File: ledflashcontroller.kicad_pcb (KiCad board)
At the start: 2 copper layers, 100 x 100 mm, 72 parts, among them J1 Conn_02x08_Odd_Even, J2 CONN_01X02, J3 CONN_01X02, J4 Conn_01x02, K1 LDD-1000H, K2 LDD-1000H, P1 V_IN, P10 BNC, P11 BNC, P12 BNC, P2 I2C_HEADER, P3 GPIO_HEADER, P4 V_DIM1, P5 V_DIM2, P6 V_OUT, P7 BNC, P8 BNC, P9 BNC, Q1 IRLML6244, Q2 IRFB3256, U1 Teensy3.6, U10 DMC2700, U11 DS3231, U2 ISO1540, U3 DMC2700, U4 DMC2700, U5 ISO1540, U6 DMC2700, U7 DMC2700, U8 ISO1540, U9 DMC2700

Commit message: Minor change in wireing
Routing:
- net /TRIG_IO1: track 59.8 -> 37.7 mm, vias 1 -> 3
- net GND: track 693.8 -> 692.6 mm
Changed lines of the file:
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@@
     (links 224)
     (no_connects 0)
-    (area 29.924999 29.924999 130.075001 130.075001)
+    (area 29.664999 26.418399 142.064286 151.875001)
     (thickness 1.6)
     (drawings 8)
-    (tracks 998)
+    (tracks 997)
     (zones 0)
     (modules 72)
@@
     (add_net GND)
   )
+  (module lib_fp:LDD-1000H (layer F.Cu)
+    (at 48.16 62.12 90)
+    (descr LDD-1000H)
+    (tags "Relay or Contactor")
+    (fp_text reference K1 (at -0.44814 0.04874 90) (layer F.SilkS)
+      (effects (font (size 1.27 1.27) (thickness 0.254)))
+    )
+    (fp_text value LDD-1000H (at -0.44814 0.04874 90) (layer F.SilkS) hide
+      (effects (font (size 1.27 1.27) (thickness 0.254)))
+    )
+    (fp_line (start -10.15 -15.9) (end 10.15 -15.9) (layer Dwgs.User) (width 0.254))
+    (fp_line (start 10.15 -15.9) (end 10.15 15.9) (layer Dwgs.User) (width 0.254))
+    (fp_line (start 10.15 15.9) (end -10.15 15.9) (layer Dwgs.User) (width 0.254))
+    (fp_line (start -10.15 15.9) (end -10.15 -15.9) (layer Dwgs.User) (width 0.254))
+    (fp_line (start -10.15 15.9) (end -10.15 -15.9) (layer F.SilkS) (width 0.254))
+    (fp_line (start -10.15 -15.9) (end 10.15 -15.9) (layer F.SilkS) (width 0.254))
+    (fp_line (start 10.15 -15.9) (end 10.15 15.9) (layer F.SilkS) (width 0.254))
+    (fp_line (start 10.15 15.9) (end -10.15 15.9) (layer F.SilkS) (width 0.254))
+    (fp_circle (center -11.382 -14.057) (end -11.55687 -14.057) (layer F.SilkS) (width 0.254))
+    (pad 1 thru_hole circle (at -7.62 -13.84 180) (size 1.3 1.3) (drill 0.8) (layers *.Cu *.Mask F.SilkS)
+      (net 2 GND))
+    (pad 1 thru_hole circle (at -7.62 -11.3 180) (size 1.3 1.3) (drill 0.8) (layers *.Cu *.Mask F.SilkS)
+      (net 2 GND))
+    (pad 23 thru_hole circle (at 7.62 -13.84 180) (size 1.3 1.3) (drill 0.8) (layers *.Cu *.Mask F.SilkS)
+      (net 16 +48V))
+    (pad 23 thru_hole circle (at 7.62 -11.3 180) (size 1.3 1.3) (drill 0.8) (layers *.Cu *.Mask F.SilkS)
+      (net 16 +48V))
+    (pad 22 thru_hole circle (at 7.62 -8.76 180) (size 1.3 1.3) (drill 0.8) (layers *.Cu *.Mask F.SilkS)
+      (net 3 "Net-(K1-Pad22)"))
+    (pad 11 thru_hole circle (at -7.62 11.3 180) (size 1.3 1.3) (drill 0.8) (layers *.Cu *.Mask F.SilkS)
+      (net 4 "Net-(K1-Pad11)"))
+    (pad 11 thru_hole circle (at -7.62 13.84 180) (size 1.3 1.3) (drill 0.8) (layers *.Cu *.Mask F.SilkS)
+      (net 4 "Net-(K1-Pad11)"))
+    (pad 13 thru_hole circle (at 7.62 11.3 180) (size 1.3 1.3) (drill 0.8) (layers *.Cu *.Mask F.SilkS)
+      (net 5 "Net-(K1-Pad13)"))
+    (pad 13 thru_hole circle (at 7.62 13.84 180) (size 1.3 1.3) (drill 0.8) (layers *.Cu *.Mask F.SilkS)
+      (net 5 "Net-(K1-Pad13)"))
+  )
   (module lib_fp:Teensy35_36_no_center (layer F.Cu)
     (at 62.09 88.62)
@@
     )
   )
-  (module lib_fp:LDD-1000H (layer F.Cu)
-    (at 48.16 62.12 90)
-    (descr LDD-1000H)
-    (tags "Relay or Contactor")
-    (fp_text reference K1 (at -0.44814 0.04874 90) (layer F.SilkS)
-      (effects (font (size 1.27 1.27) (thickness 0.254)))
-    )
-    (fp_text value LDD-1000H (at -0.44814 0.04874 90) (layer F.SilkS) hide
-      (effects (font (size 1.27 1.27) (thickness 0.254)))
-    )
-    (fp_line (start -10.15 -15.9) (end 10.15 -15.9) (layer Dwgs.User) (width 0.254))
-    (fp_line (start 10.15 -15.9) (end 10.15 15.9) (layer Dwgs.User) (width 0.254))
-    (fp_line (start 10.15 15.9) (end -10.15 15.9) (layer Dwgs.User) (width 0.254))
-    (fp_line (start -10.15 15.9) (end -10.15 -15.9) (layer Dwgs.User) (width 0.254))
-    (fp_line (start -10.15 15.9) (end -10.15 -15.9) (layer F.SilkS) (width 0.254))
-    (fp_line (start -10.15 -15.9) (end 10.15 -15.9) (layer F.SilkS) (width 0.254))
-    (fp_line (start 10.15 -15.9) (end 10.15 15.9) (layer F.SilkS) (width 0.254))
-    (fp_line (start 10.15 15.9) (end -10.15 15.9) (layer F.SilkS) (width 0.254))
-    (fp_circle (center -11.382 -14.057) (end -11.55687 -14.057) (layer F.SilkS) (width 0.254))
-    (pad 1 thru_hole circle (at -7.62 -13.84 180) (size 1.3 1.3) (drill 0.8) (layers *.Cu *.Mask F.SilkS)
-      (net 2 GND))
-    (pad 1 thru_hole circle (at -7.62 -11.3 180) (size 1.3 1.3) (drill 0.8) (layers *.Cu *.Mask F.SilkS)
-      (net 2 GND))
-    (pad 23 thru_hole circle (at 7.62 -13.84 180) (size 1.3 1.3) (drill 0.8) (layers *.Cu *.Mask F.SilkS)
-      (net 16 +48V))
-    (pad 23 thru_hole circle (at 7.62 -11.3 180) (size 1.3 1.3) (drill 0.8) (layers *.Cu *.Mask F.SilkS)
-      (net 16 +48V))
-    (pad 22 thru_hole circle (at 7.62 -8.76 180) (size 1.3 1.3) (drill 0.8) (layers *.Cu *.Mask F.SilkS)
-      (net 3 "Net-(K1-Pad22)"))
-    (pad 11 thru_hole circle (at -7.62 11.3 180) (size 1.3 1.3) (drill 0.8) (layers *.Cu *.Mask F.SilkS)
-      (net 4 "Net-(K1-Pad11)"))
-    (pad 11 thru_hole circle (at -7.62 13.84 180) (size 1.3 1.3) (drill 0.8) (layers *.Cu *.Mask F.SilkS)
-      (net 4 "Net-(K1-Pad11)"))
-    (pad 13 thru_hole circle (at 7.62 11.3 180) (size 1.3 1.3) (drill 0.8) (layers *.Cu *.Mask F.SilkS)
-      (net 5 "Net-(K1-Pad13)"))
-    (pad 13 thru_hole circle (at 7.62 13.84 180) (size 1.3 1.3) (drill 0.8) (layers *.Cu *.Mask F.SilkS)
-      (net 5 "Net-(K1-Pad13)"))
-  )
   (module Resistors_SMD:R_1206_HandSoldering (layer F.Cu)
     (at 124 107)
@@
   (segment (start 44 108.95) (end 44 111) (width 0.4) (layer F.Cu) (net 1))
   (via (at 44 111) (size 0.6) (drill 0.4) (layers F.Cu B.Cu) (net 1))
+  (segment (start 48.5 73) (end 42.526329 73) (width 0.5) (layer F.Cu) (net 2))
+  (segment (start 42.526329 73) (end 42.519521 72.993192) (width 0.5) (layer F.Cu) (net 2))
+  (segment (start 42.519521 72.568928) (end 42.519521 72.993192) (width 0.5) (layer B.Cu) (net 2))
+  (segment (start 42.519521 54.685479) (end 42.519521 72.568928) (width 0.5) (layer B.Cu) (net 2))
+  (segment (start 47.3 49.905) (end 42.519521 54.685479) (width 0.5) (layer B.Cu) (net 2))
+  (segment (start 47.3 47.5) (end 47.3 49.905) (width 0.5) (layer B.Cu) (net 2))
+  (via (at 42.519521 72.993192) (size 0.6) (drill 0.4) (layers F.Cu B.Cu) (net 2))
   (segment (start 36.86 69.74) (end 34.32 69.74) (width 0.5) (layer B.Cu) (net 2))
   (segment (start 32.88 96.24) (end 32.88 94.94) (width 0.5) (layer B.Cu) (net 2))
@@
   (segment (start 107.8 105.3) (end 104.5 102) (width 0.5) (layer F.Cu) (net 2))
   (via (at 104.5 102) (size 0.6) (drill 0.4) (layers F.Cu B.Cu) (net 2))
-  (segment (start 48.5 73) (end 43.5 73) (width 0.5) (layer F.Cu) (net 2))
-  (segment (start 43.5 73) (end 43 73) (width 0.5) (layer F.Cu) (net 2))
-  (segment (start 42 73) (end 43.5 73) (width 0.5) (layer F.Cu) (net 2))
-  (segment (start 42 70) (end 42 73) (width 0.5) (layer B.Cu) (net 2))
-  (via (at 42 73) (size 0.6) (drill 0.4) (layers F.Cu B.Cu) (net 2))
-  (segment (start 42 55.205) (end 42 70) (width 0.5) (layer B.Cu) (net 2))
-  (segment (start 47.3 47.5) (end 47.3 49.905) (width 0.5) (layer B.Cu) (net 2))
-  (segment (start 47.3 49.905) (end 42 55.205) (width 0.5) (layer B.Cu) (net 2))
   (segment (start 34.06 70) (end 34.32 69.74) (width 0.5) (layer F.Cu) (net 2))
   (segment (start 37.12 70) (end 36.86 69.74) (width 0.5) (layer F.Cu) (net 2))
@@
   (segment (start 55.684362 75.98301) (end 60.701352 81) (width 0.4) (layer B.Cu) (net 63))
   (segment (start 60.701352 81) (end 60.82 81) (width 0.4) (layer B.Cu) (net 63))
-  (segment (start 43.04 81) (end 43.04 76.54) (width 0.4) (layer F.Cu) (net 64))
-  (segment (start 43.04 76.54) (end 43 76.5) (width 0.4) (layer F.Cu) (net 64))
-  (segment (start 43 76.5) (end 32.969979 76.5) (width 0.4) (layer F.Cu) (net 64))
-  (segment (start 50.700001 56.200001) (end 51 56.5) (width 0.4) (layer F.Cu) (net 64))
-  (segment (start 32.969979 76.5) (end 32.700001 76.230022) (width 0.4) (layer F.Cu) (net 64))
-  (segment (start 32.700001 76.230022) (end 32.700001 53.973997) (width 0.4) (layer F.Cu) (net 64))
-  (segment (start 32.700001 53.973997) (end 33.623999 53.049999) (width 0.4) (layer F.Cu) (net 64))
-  (segment (start 33.623999 53.049999) (end 47.549999 53.049999) (width 0.4) (layer F.Cu) (net 64))
-  (segment (start 47.549999 53.049999) (end 50.700001 56.200001) (width 0.4) (layer F.Cu) (net 64))
+  (segment (start 51 56.5) (end 44 56.5) (width 0.4) (layer F.Cu) (net 64))
+  (segment (start 41.5 56.5) (end 44 56.5) (width 0.4) (layer F.Cu) (net 64))
+  (segment (start 44 56.5) (end 43.464745 56.5) (width 0.4) (layer F.Cu) (net 64))
+  (segment (start 42 78.5) (end 41.5 78) (width 0.4) (layer B.Cu) (net 64))
+  (via (at 41.5 56.5) (size 0.6) (drill 0.4) (layers F.Cu B.Cu) (net 64))
+  (segment (start 41.5 78) (end 41.5 56.5) (width 0.4) (layer B.Cu) (net 64))
+  (segment (start 43.04 81) (end 43.04 79.54) (width 0.4) (layer F.Cu) (net 64))
+  (segment (start 43.04 79.54) (end 42 78.5) (width 0.4) (layer F.Cu) (net 64))
+  (via (at 42 78.5) (size 0.6) (drill 0.4) (layers F.Cu B.Cu) (net 64))
   (segment (start 53.5 56.42) (end 51.08 56.42) (width 0.4) (layer B.Cu) (net 64))
   (segment (start 51.08 56.42) (end 51 56.5) (width 0.4) (layer B.Cu) (net 64))
   (via (at 51 56.5) (size 0.6) (drill 0.4) (layers F.Cu B.Cu) (net 64))
-  (segment (start 53.5 57.5) (end 41 57.5) (width 0.4) (layer F.Cu) (net 65))
-  (segment (start 40.5 81) (end 40.5 58) (width 0.4) (layer B.Cu) (net 65))
-  (segment (start 40.5 58) (end 41 57.5) (width 0.4) (layer B.Cu) (net 65))
-  (via (at 41 57.5) (size 0.6) (drill 0.4) (layers F.Cu B.Cu) (net 65))
+  (segment (start 40.5 81) (end 40.5 57.588079) (width 0.4) (layer B.Cu) (net 65))
+  (segment (start 53.5 57.5) (end 40.588079 57.5) (width 0.4) (layer F.Cu) (net 65))
+  (via (at 40.588079 57.5) (size 0.6) (drill 0.4) (layers F.Cu B.Cu) (net 65))
+  (segment (start 40.5 57.588079) (end 40.588079 57.5) (width 0.4) (layer B.Cu) (net 65))
   (segment (start 53.5 58.96) (end 53.5 57.5) (width 0.4) (layer B.Cu) (net 65))
   (via (at 53.5 57.5) (size 0.6) (drill 0.4) (layers F.Cu B.Cu) (net 65))

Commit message: Minor change in wiring again
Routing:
- net +3V3: track 192.1 -> 184.8 mm, vias 2 -> 3
- net /TRIG_IO7: track 25.6 -> 23.2 mm, vias 1 -> 0
- net /TRIG_IO6: track 25.6 -> 23.5 mm, vias 1 -> 0
- net +5V: track 240.9 -> 242.5 mm, vias 19 -> 17
- net +48V: track 151.7 -> 152.6 mm
- net GND: track 692.6 -> 693.0 mm, vias 19 -> 18

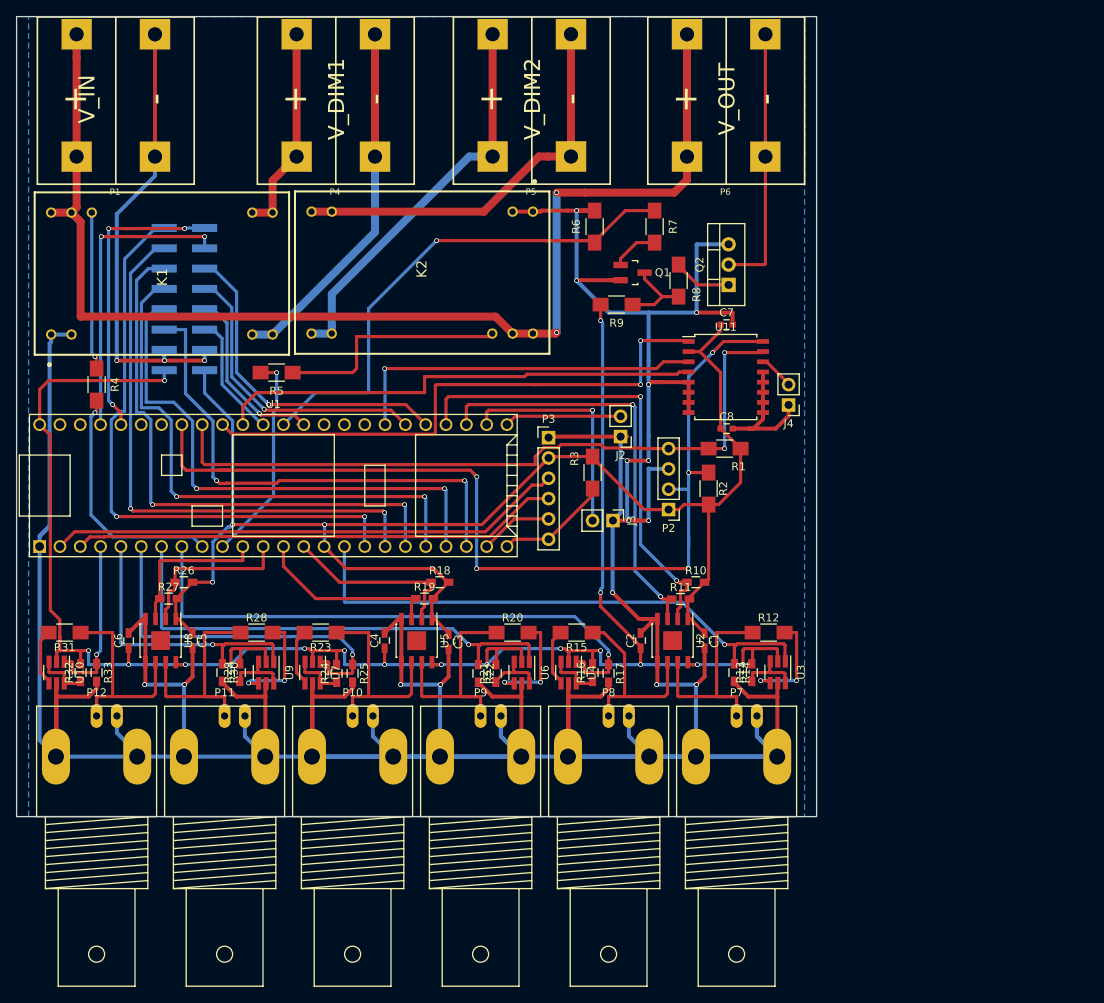
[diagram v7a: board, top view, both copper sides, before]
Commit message: Added groundplane
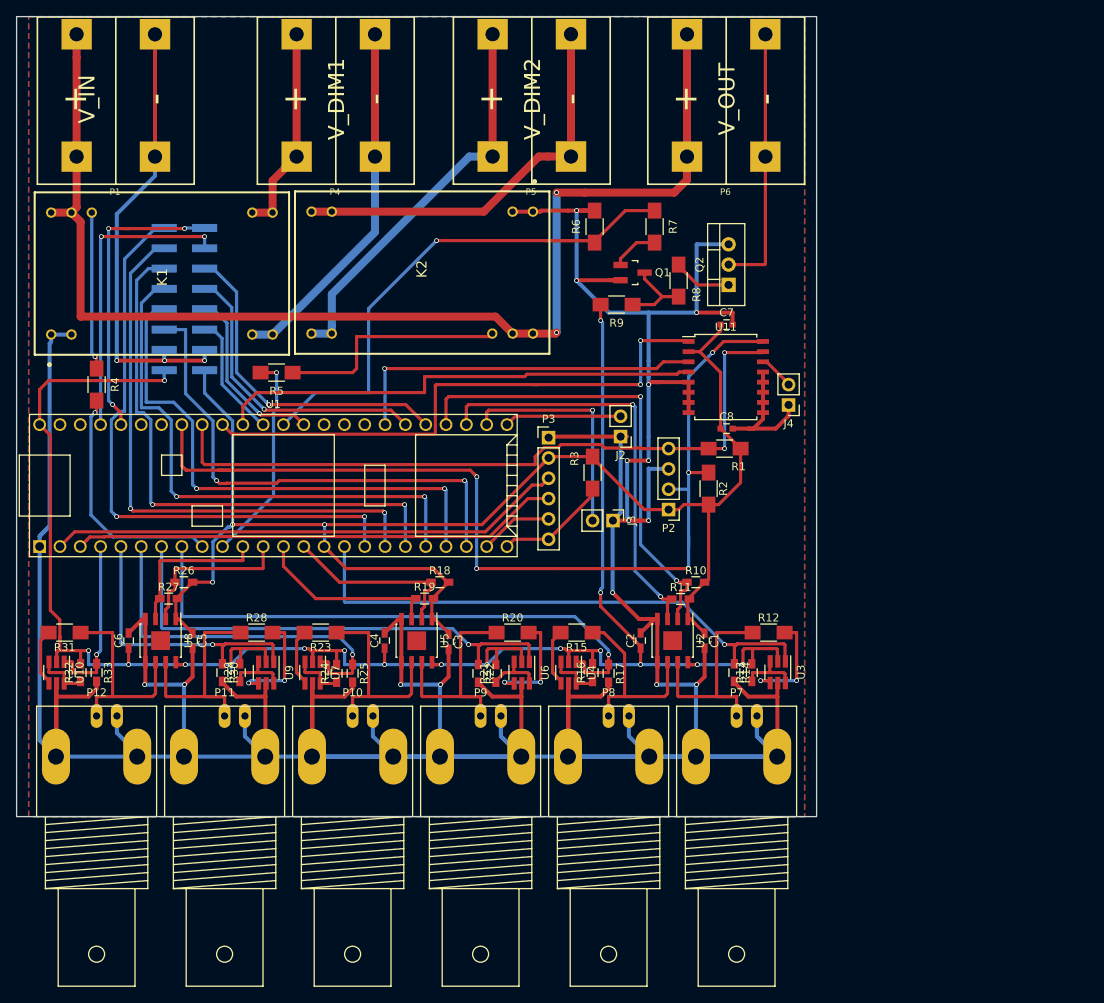
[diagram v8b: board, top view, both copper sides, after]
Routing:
- added copper zone on F.Cu, net GND
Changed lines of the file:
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@@
+    )
+  )
+  (zone (net 2) (net_name GND) (layer F.Cu) (hatch edge 0.508)
+    (connect_pads (clearance 1))
+    (min_thickness 0.254)
+    (fill yes (arc_segments 16) (thermal_gap 0.508) (thermal_bridge_width 0.508))
+    (polygon
+      (pts
+        (xy 31.5 30) (xy 128.5 30) (xy 128.5 130) (xy 75 130) (xy 40 130)
+        (xy 31.5 130)
+      )
     )
   )
